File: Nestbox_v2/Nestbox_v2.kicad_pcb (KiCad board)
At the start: 2 copper layers, 85 x 60 mm, 109 parts, among them CON301 Micro_SD_Card, J201 BATT_CONN_01X02, J401 LB_DETECT_CONN_01X04, J402 CONN_01X05, J501 CONN_01X01, J502 CONN_01X06, J601 LOAD_CELL_CONN_01X04, J701 RFID_CONN_01X05, P301 RX/TX, P302 TST/RST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

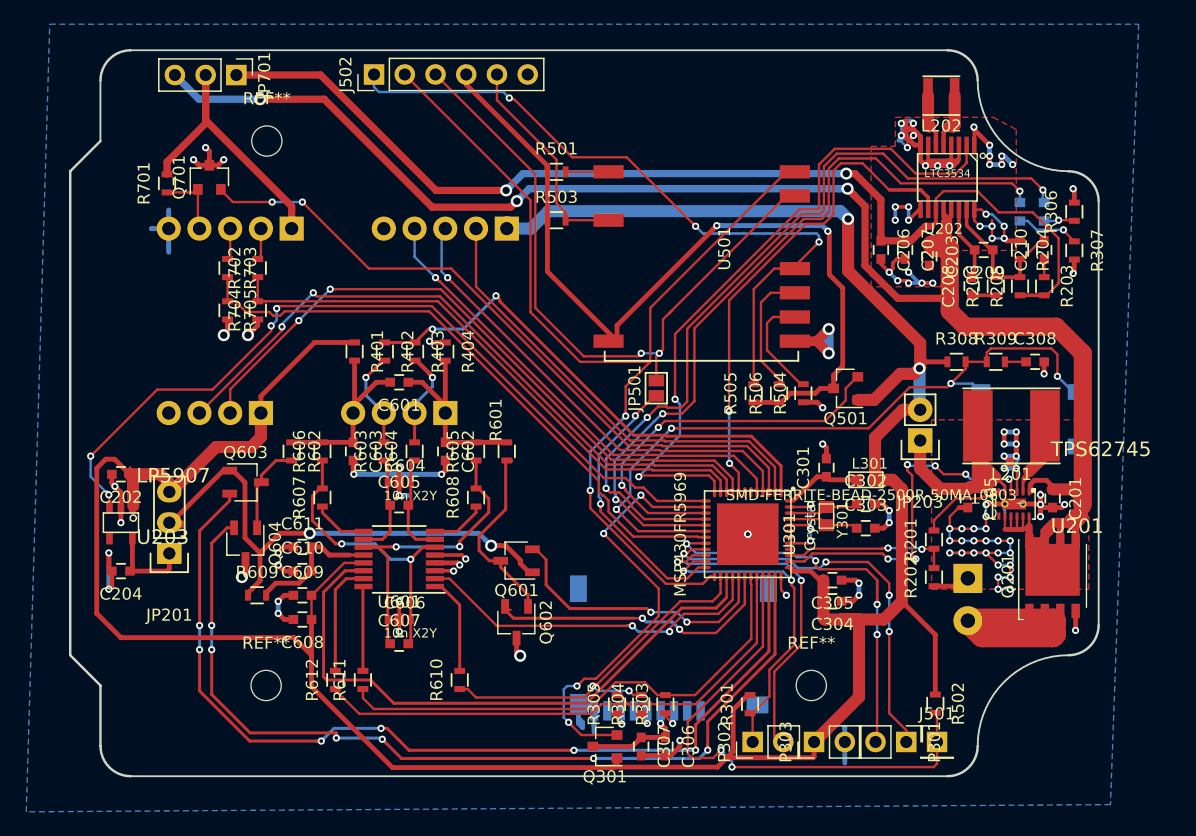
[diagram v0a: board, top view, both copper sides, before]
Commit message: finished silkscreen
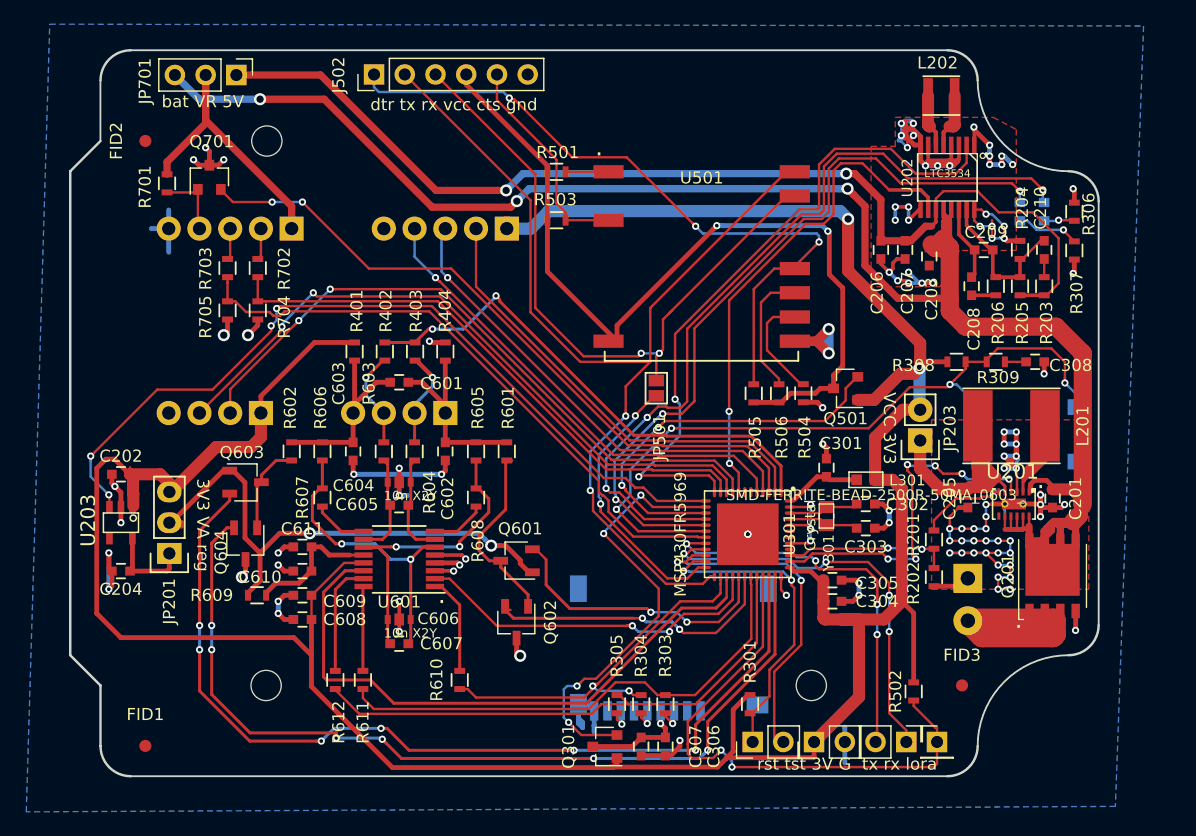
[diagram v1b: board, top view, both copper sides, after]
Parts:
- added FID1: Fiducial_1mm_Dia_2.54mm_Outer_CopperTop, Fiducials:Fiducial_1mm_Dia_2.54mm_Outer_CopperTop, F.Cu at (38.7, 185.0)
- added FID2: Fiducial_1mm_Dia_2.54mm_Outer_CopperTop, Fiducials:Fiducial_1mm_Dia_2.54mm_Outer_CopperTop, F.Cu at (38.7, 135.0)
- added FID3: Fiducial_1mm_Dia_2.54mm_Outer_CopperTop, Fiducials:Fiducial_1mm_Dia_2.54mm_Outer_CopperTop, F.Cu at (106.2, 180.0)
- added G***: LOGO, Octanis3:octanis3_logo, B.Cu at (110.2, 149.0)
- added G***: LOGO, Octanis3:VogelwarteLogo3, B.Cu at (77.7, 154.0)
- added G***: LOGO, Octanis3:octanis_open_incubator_logo, B.Cu at (90.7, 154.0)
- added REF***: OSHW-Logo2_9.8x8mm_SilkScreen, Symbols:OSHW-Logo2_9.8x8mm_SilkScreen, B.Cu at (59.7, 177.0)
- moved R502 2.05 mm to (102.2, 180.5)
- moved SW301 1.25 mm to (111.7, 159.2)
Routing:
- net /Control/LORA_RESET_N: track 43.5 -> 45.4 mm
- net +3V3: track 244.7 -> 243.0 mm
- net /Control/DBG_Switch: track 59.1 -> 60.4 mm
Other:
- board text added: "+"
- board text added: "."
- board text added: "3V3 VA reg"
- board text added: "4 x NiMh 3.6 - 6 V"
- board text added: "BAT"
- board text added: "Digital Nestbox v2.0 by"
- board text added: "EXC-A IN2 IN1 EXC-B"
- board text added: "LB_IN"
- board text added: "Micro SD card"
- board text added: "PIR"
- board text added: "RFID"
- board text added: "VCC 3V3"
- board text added: "VDD CLK DATA SLEEP GND"
- board text added: "VDD EN PIR1 PIR2 GND"
- board text added: "VDD LB1 LB2 G"
- board text added: "WEIGHT/ LB_OUT"
- board text added: "WIFI"
- board text added: "bat VR 5V"
- board text added: "data"
- board text added: "dtr tx rx vcc cts gnd"
- board text added: "in collaboration with"
- board text added: "nestbox.octanis.org June 2018 Tschui/Wüthrich"
- board text added: "rst tst 3V G tx rx lora"
- board text added: "start"
- board text added: "status"

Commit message: corrected transistor pins
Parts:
- Q301, Q501: footprint TO_SOT_Packages_SMD:SOT-23 -> TO_SOT_Packages_SMD:TSOT-23
- Q701: value Q_NMOS_DGS -> Q_NMOS_GSD; footprint TO_SOT_Packages_SMD:SOT-23 -> TO_SOT_Packages_SMD:TSOT-23
- moved Q501 0.77 mm to (97.2, 155.0), turned to 270 degrees
- moved Q301 0.33 mm to (77.0, 185.0), turned to 0 degrees
- moved Q701 0.29 mm to (43.7, 138.0), turned to 270 degrees
- turned Q601 to 270 degrees
- turned Q603 to 90 degrees
- turned Q604 to 90 degrees
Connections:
- Q301 pad 1: +3V3 -> /Control/SD_CARD_ENABLE
- Q301 pad 2: /Control/SD_CARD_ENABLE -> Net-(C306-Pad1)
- Q301 pad 3: Net-(C306-Pad1) -> +3V3
- Q501 pad 1: +3V3 -> /Communication/ESP12_ENABLE
- Q501 pad 2: /Communication/ESP12_ENABLE -> /Communication/ESP12_VCC
- Q501 pad 3: /Communication/ESP12_VCC -> +3V3
- Q601 pad 1: VAA -> /Load_Cell/EXC_A_P
- Q601 pad 2: /Load_Cell/EXC_A_P -> Net-(Q601-Pad2)
- Q601 pad 3: Net-(Q601-Pad3) -> VAA
- Q602 pad 1: Net-(Q601-Pad3) -> /Load_Cell/EXC_A_N
- Q602 pad 2: /Load_Cell/EXC_A_N -> GND
- Q602 pad 3: GND -> Net-(Q601-Pad2)
- Q603 pad 1: VAA -> /Load_Cell/EXC_B_P
- Q603 pad 2: /Load_Cell/EXC_B_P -> Net-(Q603-Pad2)
- Q603 pad 3: Net-(Q603-Pad3) -> VAA
- Q604 pad 1: Net-(Q603-Pad3) -> /Load_Cell/EXC_B_N
- Q604 pad 2: /Load_Cell/EXC_B_N -> GND
- Q604 pad 3: GND -> Net-(Q603-Pad2)
- Q701 pad 1: Net-(J701-Pad4) -> /Control/RFID_SLEEP_N
- Q701 pad 2: /Control/RFID_SLEEP_N -> GND
- Q701 pad 3: GND -> Net-(J701-Pad4)
- R601 pad 2: Net-(Q601-Pad3) -> Net-(Q601-Pad2)
- R602 pad 2: Net-(Q603-Pad3) -> Net-(Q603-Pad2)
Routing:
- net Net-(Q601-Pad2): track 0.00 -> 16.4 mm
- net Net-(Q601-Pad3): track 16.0 -> 0.00 mm
- net Net-(Q603-Pad2): track 0.00 -> 7.63 mm
- net Net-(Q603-Pad3): track 7.50 -> 0.00 mm
- net /Load_Cell/EXC_B_N: track 75.3 -> 72.1 mm
- net /Control/LOADCELL_SPI_CS: track 30.1 -> 32.9 mm
- net VAA: track 44.7 -> 47.3 mm
- net /Load_Cell/EXC_A_N: track 24.6 -> 22.1 mm
- net GND: track 225.6 -> 223.1 mm, vias 111 -> 109
- net /Control/RFID_SLEEP_N: track 56.9 -> 59.3 mm
- net /Control/SD_CARD_ENABLE: track 36.6 -> 34.6 mm
- net +3V3: track 243.0 -> 244.9 mm
- net /Communication/ESP12_ENABLE: track 32.8 -> 33.9 mm
- net /Load_Cell/EXC_A_P: track 23.6 -> 22.9 mm
- net /Communication/ESP12_VCC: track 70.4 -> 69.8 mm
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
